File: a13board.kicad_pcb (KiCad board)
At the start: 4 copper layers, 49.8 x 45.7 mm, 124 parts, among them U1 H27UBG8T2A/TSOP48, U2 A13, U3 H5TQ2G43CFR, U4 H5TQ2G43CFR, U5 OLIMEX_IC_AXP209, U6 SY8008BAAC, U7 SY8008BAAC

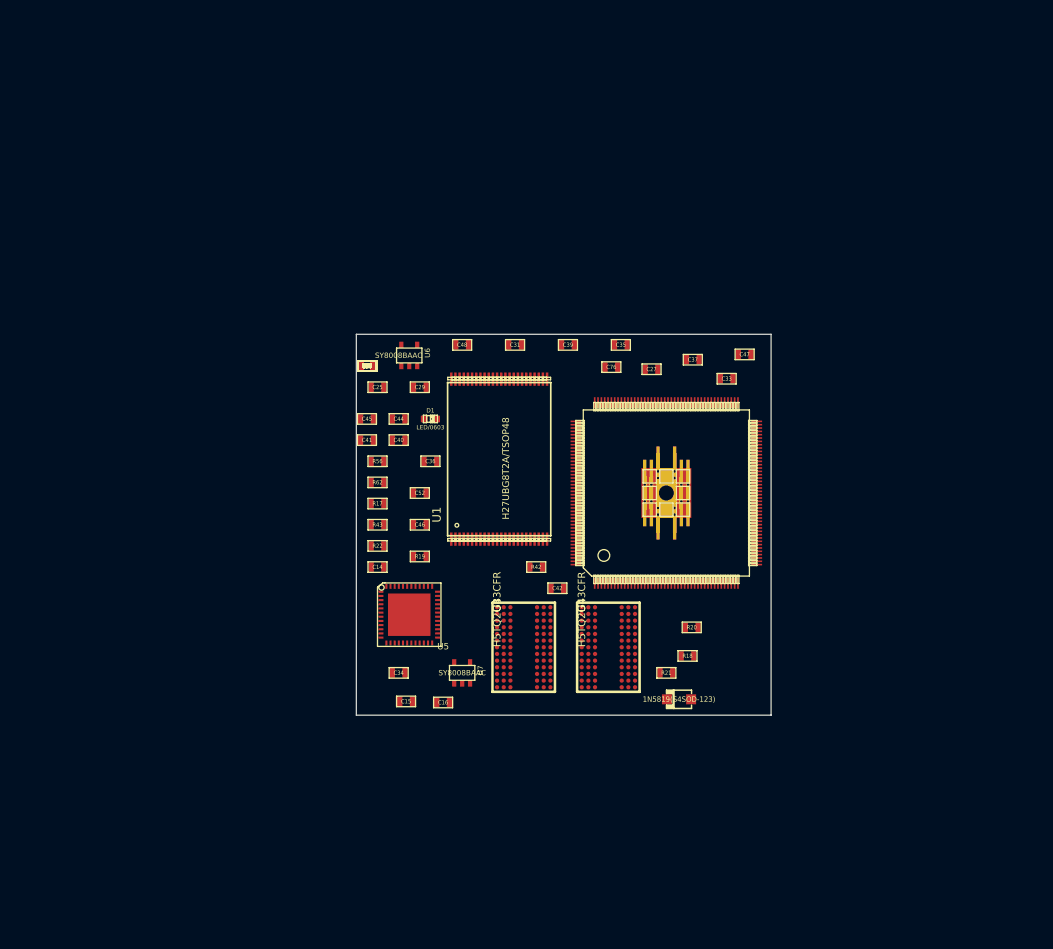
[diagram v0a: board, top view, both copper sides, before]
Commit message: fixed schematics errors, added CD32 and 4x0402 packages, started layout
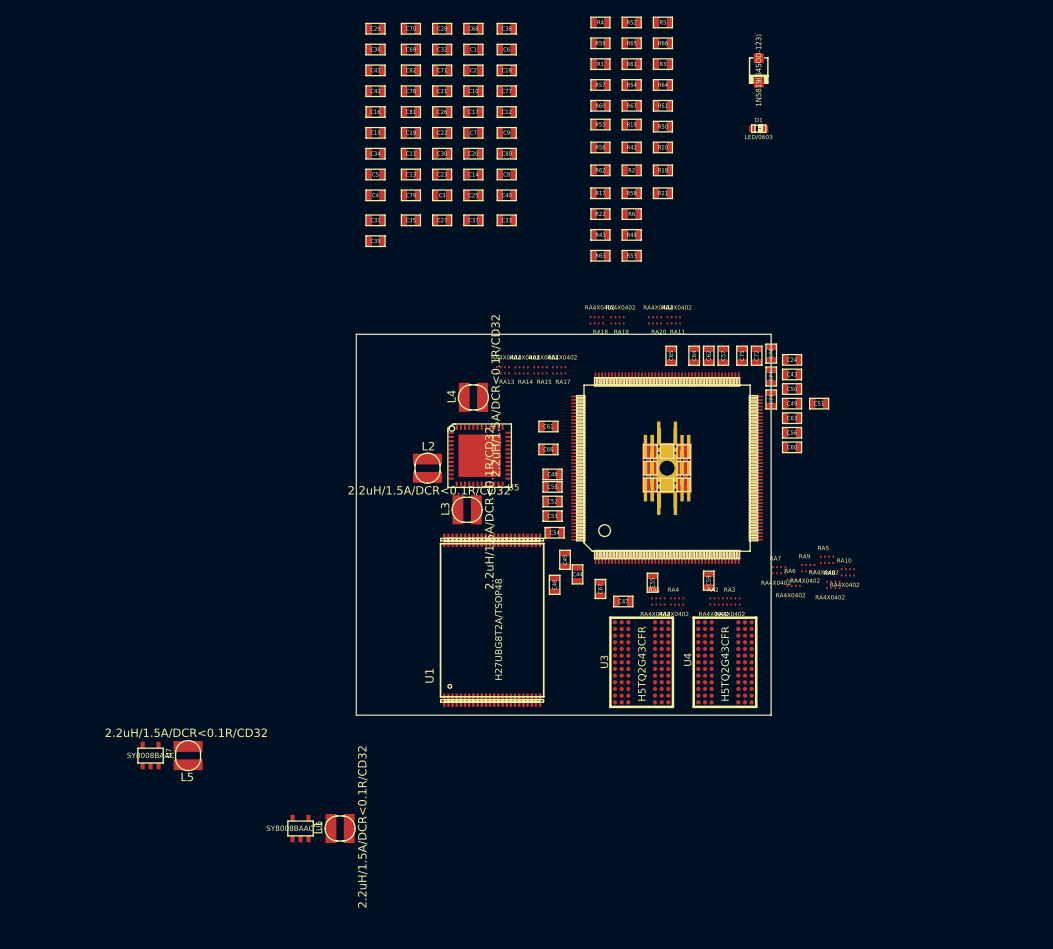
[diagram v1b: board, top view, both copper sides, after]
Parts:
- added L1: 2.2uH/1.5A/DCR<0.1R/CD32, CD32, F.Cu at (74.2, 134.2)
- added L2: 2.2uH/1.5A/DCR<0.1R/CD32, CD32, F.Cu at (84.8, 91.0)
- added L3: 2.2uH/1.5A/DCR<0.1R/CD32, CD32, F.Cu at (89.5, 96.0)
- added L4: 2.2uH/1.5A/DCR<0.1R/CD32, CD32, F.Cu at (90.2, 82.5)
- added L5: 2.2uH/1.5A/DCR<0.1R/CD32, CD32, F.Cu at (56.0, 125.5)
- added RA1: RA4X0402, RN4x0402, F.Cu at (112.5, 107.0)
- added RA10: RA4X0402, RN4x0402, F.Cu at (135.2, 103.5)
- added RA11: RA4X0402, RN4x0402, F.Cu at (114.2, 73.2)
- added RA13: RA4X0402, RN4x0402, F.Cu at (93.8, 79.2)
- added RA14: RA4X0402, RN4x0402, F.Cu at (96.0, 79.2)
- added RA15: RA4X0402, RN4x0402, F.Cu at (98.2, 79.2)
- added RA17: RA4X0402, RN4x0402, F.Cu at (100.5, 79.2)
- added RA18: RA4X0402, RN4x0402, F.Cu at (105.0, 73.2)
- added RA19: RA4X0402, RN4x0402, F.Cu at (107.5, 73.2)
- added RA2: RA4X0402, RN4x0402, F.Cu at (119.5, 107.0)
- added RA20: RA4X0402, RN4x0402, F.Cu at (112.0, 73.2)
- added RA3: RA4X0402, RN4x0402, F.Cu at (121.5, 107.0)
- added RA4: RA4X0402, RN4x0402, F.Cu at (114.8, 107.0)
- added RA5: RA4X0402, RN4x0402, F.Cu at (132.8, 102.0)
- added RA6: RA4X0402, RN4x0402, F.Cu at (128.8, 104.8)
- added RA7: RA4X0402, RN4x0402, F.Cu at (127.0, 103.2)
- added RA8: RA4X0402, RN4x0402, F.Cu at (133.5, 105.0)
- added RA9: RA4X0402, RN4x0402, F.Cu at (130.5, 103.0)
- moved D2 76.1 mm to (124.5, 43.2), turned to 90 degrees
- moved C16 71.3 mm to (78.5, 48.2)
- moved C15 68.3 mm to (78.5, 50.8)
- moved C42 63.5 mm to (78.5, 45.8), turned to 180 degrees
- moved C34 62.4 mm to (78.5, 53.2)
- moved R18 58.4 mm to (113.0, 55.2)
- moved U6 58.3 mm to (69.5, 134.2)
- moved R19 57.8 mm to (109.2, 49.8)
- moved R20 57.7 mm to (113.0, 52.5)
- moved R21 57.6 mm to (113.0, 58.0)
- moved C51 54.5 mm to (131.8, 83.2)
- moved R5 54.4 mm to (113.0, 37.5)
- moved D1 52.6 mm to (124.5, 50.2)
- moved R66 52.6 mm to (113.0, 40.0)
- moved R52 52.1 mm to (109.2, 37.5)
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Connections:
- U3 pad N8: (no net) -> /DRAM/DDR3_A8
- U4 pad N8: (no net) -> /DRAM/DDR3_A8

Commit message: Started tracing
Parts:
- moved R52 82.0 mm to (115.6, 119.3), turned to 90 degrees
- moved C2 81.5 mm to (125.6, 116.7), turned to 270 degrees
- moved C1 79.5 mm to (113.7, 116.7), turned to 270 degrees
- moved C29 78.4 mm to (65.5, 115.6), turned to 180 degrees
- moved R64 76.7 mm to (69.3, 108.1), turned to 270 degrees
- moved R66 74.6 mm to (67.9, 99.4), turned to 270 degrees
- moved C42 73.1 mm to (65.5, 117.7)
- moved C10 71.2 mm to (113.7, 113.0), turned to 90 degrees
- moved C6 69.8 mm to (122.9, 104.4), turned to 270 degrees
- moved C69 66.8 mm to (131.2, 86.7), turned to 180 degrees
- moved C68 66.6 mm to (133.9, 88.6)
- moved R56 66.6 mm to (102.9, 119.0)
- moved C9 66.4 mm to (103.6, 116.5), turned to 90 degrees
- moved C78 65.6 mm to (133.9, 86.9), turned to 180 degrees
- moved C3 65.3 mm to (115.6, 116.7), turned to 90 degrees
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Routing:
- net N-0000072: track 0.00 -> 10.4 mm
- net N-0000073: track 0.00 -> 10.1 mm
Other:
- board size 49.8 x 45.7 mm -> 99.8 x 45.7 mm
- net class Default: clearance 0.254 -> 0.1524; trace_width 0.254 -> 0.1524; via_dia 0.889 -> 0.41; via_drill 0.635 -> 0.3084
- net class signal added: clearance 0.1524, trace_width 0.1524, via_dia 0.41, via_drill 0.3084
- rule pad_to_mask_clearance: 0 -> 0.1
- rule trace_clearance: 0.254 -> 0.1524
- rule trace_min: 0.254 -> 0.1524
- rule via_min_drill: 0.508 -> 0.3
- rule via_min_size: 0.889 -> 0.4

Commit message: more tracing progress
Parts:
- C4, C44, C45, C46, C47, C48, C5, C52, C55, C56, C58, C59, C6, C60, C61, C66, C67, C68, C69, C7, C70, C78: footprint SM0603_Capa -> SM0402
- R17, R18, R19, R20, R21, R22, R42, R43, R50: footprint SM0603 -> SM0402
- moved R19 13.2 mm to (110.7, 108.0)
- moved C2 10.4 mm to (115.6, 113.9)
- moved RA3 8.43 mm to (113.2, 108.2)
- moved R42 5.51 mm to (109.9, 108.0)
- moved C54 5.33 mm to (97.3, 90.6)
- moved RA8 4.98 mm to (134.9, 102.3)
- moved D2 4.74 mm to (89.8, 93.6)
- moved R20 4.49 mm to (111.6, 108.0)
- moved C8 4.43 mm to (131.6, 94.3), turned to 315 degrees
- moved R21 4.23 mm to (117.7, 106.7)
- moved RA9 3.93 mm to (131.0, 100.6)
- moved RA1 3.58 mm to (108.5, 108.0)
- moved C47 3.42 mm to (109.8, 103.9), turned to 90 degrees
- moved R2 3.35 mm to (106.4, 107.3)
- moved C68 3.10 mm to (131.1, 87.3)
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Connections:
- net N-00000100 renamed /DRAM/CPU_BA0
- net N-00000101 renamed /DRAM/CPU_BA1
- net N-00000102 renamed /DRAM/CPU_BA2
- net N-00000103 renamed /DRAM/CPU_ODT
- net N-0000072 renamed /DRAM/CPU_CK
- net N-0000073 renamed /DRAM/CPU_CK_N
- net N-0000074 renamed /DRAM/CPU_DM1
- net N-0000075 renamed /DRAM/CPU_MEMRST
- net N-0000076 renamed /DRAM/CPU_WE
- net N-0000077 renamed /DRAM/CPU_CKE
- net N-0000078 renamed /DRAM/CPU_CAS
- net N-0000079 renamed /DRAM/CPU_RAS
- net N-0000080 renamed /DRAM/CPU_DM0
- net N-0000081 renamed /DRAM/CPU_A6
- net N-0000082 renamed /DRAM/CPU_DQS0
- net N-0000083 renamed /DRAM/CPU_DQS0_N
- net N-0000084 renamed /DRAM/CPU_DQS1
- net N-0000085 renamed /DRAM/CPU_DQS1_N
- net N-0000086 renamed /DRAM/CPU_A0
- net N-0000087 renamed /DRAM/CPU_A1
- net N-0000088 renamed /DRAM/CPU_A2
- net N-0000089 renamed /DRAM/CPU_A3
- net N-0000090 renamed /DRAM/CPU_A4
- net N-0000091 renamed /DRAM/CPU_A5
- net N-0000092 renamed /DRAM/CPU_A7
- net N-0000093 renamed /DRAM/CPU_A8
- net N-0000094 renamed /DRAM/CPU_A9
- net N-0000095 renamed /DRAM/CPU_A10
- net N-0000096 renamed /DRAM/CPU_A11
- net N-0000097 renamed /DRAM/CPU_A12
- net N-0000098 renamed /DRAM/CPU_A13
- net N-0000099 renamed /DRAM/CPU_A14
- RA1 pad 1: /DRAM/DDR3_D0 -> /DRAM/CPU_D0
- RA1 pad 2: /DRAM/DDR3_D2 -> /DRAM/CPU_D2
- RA1 pad 3: /DRAM/DDR3_D6 -> /DRAM/CPU_D6
- RA1 pad 4: /DRAM/DDR3_D4 -> /DRAM/CPU_D4
- RA1 pad 5: N-0000056 -> /DRAM/DDR3_D4
- RA1 pad 6: N-0000062 -> /DRAM/DDR3_D6
- RA1 pad 7: N-0000059 -> /DRAM/DDR3_D2
- RA1 pad 8: N-0000057 -> /DRAM/DDR3_D0
- RA2 pad 1: /DRAM/DDR3_D10 -> /DRAM/CPU_D10
- RA2 pad 2: /DRAM/DDR3_D14 -> /DRAM/CPU_D14
- RA2 pad 3: /DRAM/DDR3_D8 -> /DRAM/CPU_D8
- RA2 pad 4: /DRAM/DDR3_D12 -> /DRAM/CPU_D12
- RA2 pad 5: N-0000068 -> /DRAM/DDR3_D12
- RA2 pad 6: N-0000064 -> /DRAM/DDR3_D8
- RA2 pad 7: N-0000070 -> /DRAM/DDR3_D14
- RA2 pad 8: N-0000066 -> /DRAM/DDR3_D10
- RA3 pad 1: /DRAM/DDR3_D5 -> /DRAM/CPU_D5
- RA3 pad 2: /DRAM/DDR3_D7 -> /DRAM/CPU_D7
- RA3 pad 3: /DRAM/DDR3_D3 -> /DRAM/CPU_D3
- RA3 pad 4: /DRAM/DDR3_D1 -> /DRAM/CPU_D1
- RA3 pad 5: N-0000058 -> /DRAM/DDR3_D1
- RA3 pad 6: N-0000060 -> /DRAM/DDR3_D3
- RA3 pad 7: N-0000063 -> /DRAM/DDR3_D7
- RA3 pad 8: N-0000061 -> /DRAM/DDR3_D5
- RA4 pad 1: /DRAM/DDR3_D15 -> /DRAM/CPU_D15
- RA4 pad 2: /DRAM/DDR3_D13 -> /DRAM/CPU_D13
- RA4 pad 3: /DRAM/DDR3_D9 -> /DRAM/CPU_D9
- RA4 pad 4: /DRAM/DDR3_D11 -> /DRAM/CPU_D11
- RA4 pad 5: N-0000067 -> /DRAM/DDR3_D11
- RA4 pad 6: N-0000065 -> /DRAM/DDR3_D9
- RA4 pad 7: N-0000069 -> /DRAM/DDR3_D13
- RA4 pad 8: N-0000071 -> /DRAM/DDR3_D15
- U2 pad 19: N-0000056 -> /DRAM/CPU_D4
- U2 pad 20: N-0000062 -> /DRAM/CPU_D6
- U2 pad 21: N-0000059 -> /DRAM/CPU_D2
- U2 pad 22: N-0000057 -> /DRAM/CPU_D0
- U2 pad 24: N-0000067 -> /DRAM/CPU_D11
- U2 pad 25: N-0000065 -> /DRAM/CPU_D9
- U2 pad 26: N-0000069 -> /DRAM/CPU_D13
- U2 pad 27: N-0000071 -> /DRAM/CPU_D15
- U2 pad 36: N-0000068 -> /DRAM/CPU_D12
- U2 pad 37: N-0000064 -> /DRAM/CPU_D8
- U2 pad 38: N-0000070 -> /DRAM/CPU_D14
- U2 pad 39: N-0000066 -> /DRAM/CPU_D10
- U2 pad 40: N-0000058 -> /DRAM/CPU_D1
- U2 pad 41: N-0000060 -> /DRAM/CPU_D3
- U2 pad 42: N-0000063 -> /DRAM/CPU_D7
- U2 pad 44: N-0000061 -> /DRAM/CPU_D5
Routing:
- net /DRAM/DDR3_A7: track 0.00 -> 47.7 mm, vias 0 -> 2
- net /DRAM/DDR3_RST: track 0.00 -> 45.0 mm
- net /DRAM/DDR3_A9: track 0.00 -> 44.6 mm, vias 0 -> 2
- net /DRAM/DDR3_A5: track 0.00 -> 40.3 mm, vias 0 -> 2
- net /DRAM/DDR3_BA0: track 0.00 -> 39.3 mm, vias 0 -> 2
- net /DRAM/DDR3_A13: track 0.00 -> 39.3 mm
- net /DRAM/DDR3_A0: track 0.00 -> 38.9 mm
- net /DRAM/DDR3_A3: track 0.00 -> 38.1 mm, vias 0 -> 2
- net /DRAM/DDR3_BA2: track 0.00 -> 38.0 mm
- net /DRAM/DDR3_A2: track 0.00 -> 37.7 mm
- net /DRAM/DDR3_WE: track 0.00 -> 37.7 mm
- net /DRAM/DDR3_CAS: track 0.00 -> 35.5 mm
- net /DRAM/DDR3_RAS: track 0.00 -> 35.1 mm
- net /DRAM/DDR3_A11: track 0.00 -> 26.9 mm
- net N-00000190: track 0.00 -> 26.3 mm
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- added copper zone on Inner1.Cu, net GND
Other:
- net class Default: via_dia 0.41 -> 0.31; via_drill 0.3084 -> 0.3048
- net class bga added: clearance 0.1016, trace_width 0.1016, via_dia 0.31, via_drill 0.3048
- net class signal: via_dia 0.41 -> 0.31; via_drill 0.3084 -> 0.3048
- rule trace_min: 0.1524 -> 0.1016
- rule via_min_size: 0.4 -> 0.3048

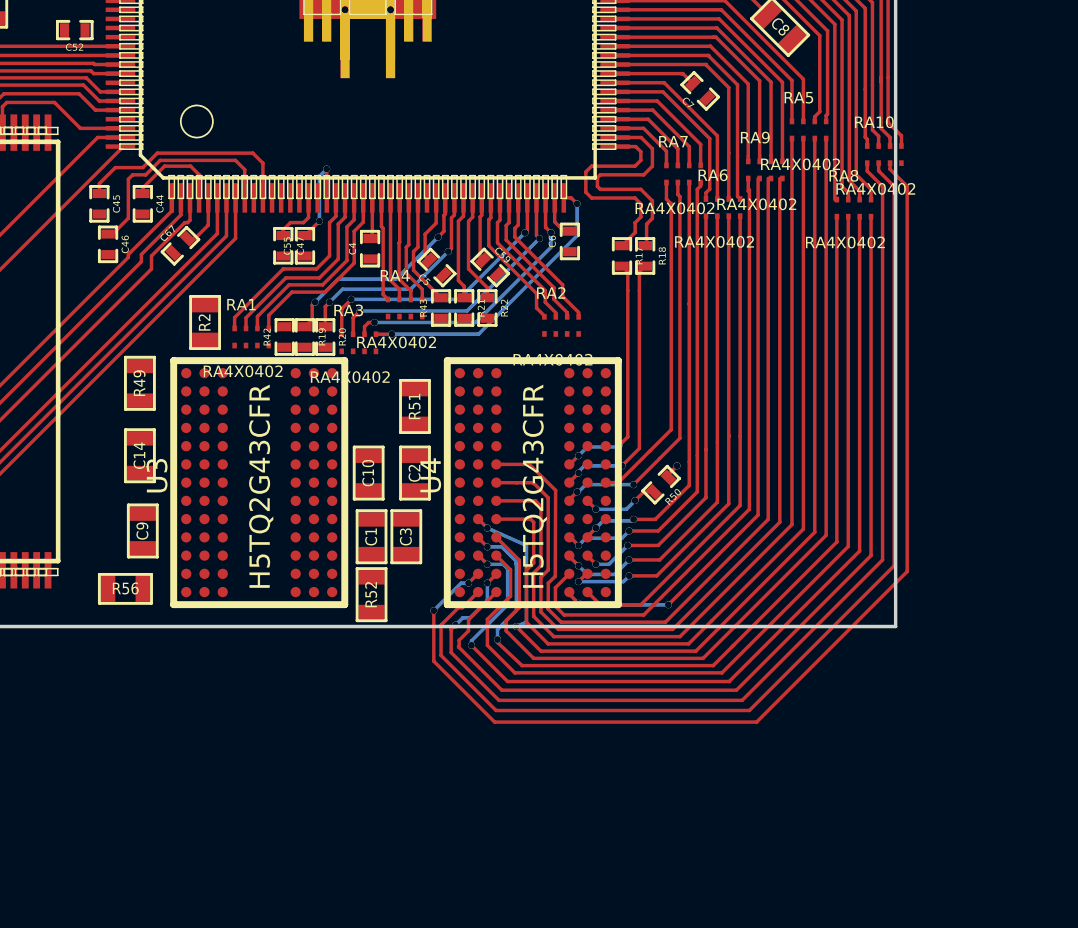
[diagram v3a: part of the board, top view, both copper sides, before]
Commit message: Re-tracing DDR3 with 4mil traces
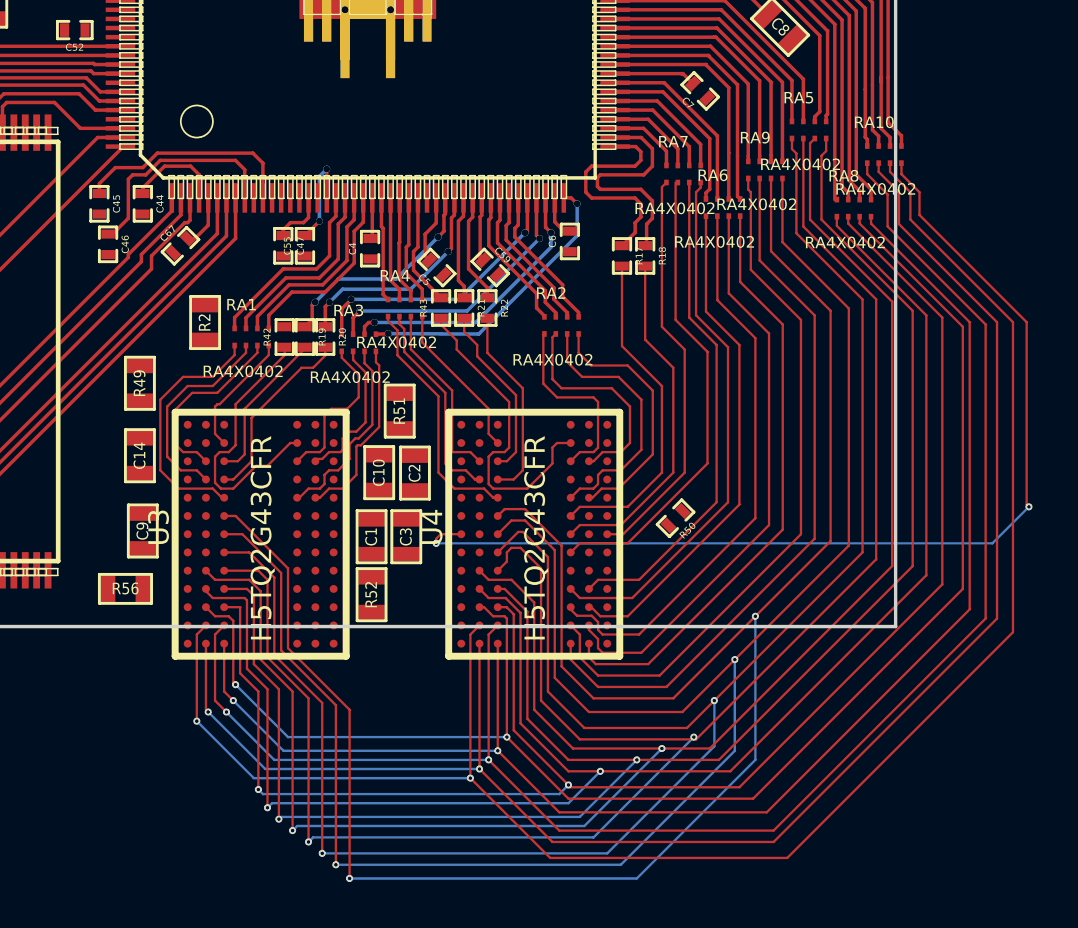
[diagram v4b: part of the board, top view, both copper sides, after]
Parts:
- moved U3 2.26 mm to (105.6, 111.8)
- moved U4 2.26 mm to (117.6, 111.8)
- moved R50 1.60 mm to (127.0, 115.9)
- moved R51 0.70 mm to (114.9, 111.2)
- moved C10 0.46 mm to (114.0, 113.9)
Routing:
- net /DRAM/DDR3_RAS: track 35.1 -> 85.8 mm, vias 0 -> 2
- net /DRAM/DDR3_CAS: track 35.5 -> 83.3 mm, vias 0 -> 2
- net /DRAM/DDR3_ODT: track 0.00 -> 45.4 mm, vias 0 -> 2
- net /DRAM/DDR3_WE: track 37.7 -> 82.8 mm, vias 0 -> 2
- net /DRAM/DDR3_BA2: track 38.0 -> 80.3 mm, vias 0 -> 2
- net /DRAM/DDR3_BA0: track 39.3 -> 79.3 mm
- net /DRAM/DDR3_A0: track 38.9 -> 76.5 mm, vias 0 -> 2
- net /DRAM/DDR3_A3: track 38.1 -> 73.5 mm
- net /DRAM/DDR3_A2: track 37.7 -> 70.2 mm, vias 0 -> 2
- net /DRAM/DDR3_A7: track 47.7 -> 76.4 mm
- net /DRAM/DDR3_A9: track 44.6 -> 71.7 mm
- net /DRAM/DDR3_A5: track 40.3 -> 67.0 mm
- net /DRAM/DDR3_RST: track 45.0 -> 71.7 mm, vias 0 -> 2
- net /DRAM/DDR3_A13: track 39.3 -> 64.4 mm, vias 0 -> 2
- net /DRAM/DDR3_DM1: track 0.00 -> 14.1 mm
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- removed copper zone on Inner1.Cu, net GND
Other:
- net class Default: clearance 0.1524 -> 0.15; trace_width 0.1524 -> 0.15; via_drill 0.3048 -> 0.3
- net class bga: via_drill 0.3048 -> 0.3
- net class signal removed
- rule trace_clearance: 0.1524 -> 0.15
- rule via_min_size: 0.3048 -> 0.3

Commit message: still routing ddr3
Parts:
- moved L5 11.4 mm to (74.7, 101.0)
- moved C40 11.1 mm to (80.0, 104.5)
- moved R66 11.1 mm to (77.9, 104.5)
- moved U7 11.1 mm to (79.5, 101.0)
- moved R67 10.5 mm to (83.4, 101.0)
- moved C39 8.39 mm to (85.7, 101.0)
- moved C41 7.82 mm to (85.7, 103.9)
- moved R56 7.81 mm to (95.1, 120.0)
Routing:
- net /DRAM/DDR3_A7: track 76.4 -> 0.00 mm, vias 2 -> 0
- net /DRAM/DDR3_A9: track 71.7 -> 0.00 mm, vias 2 -> 0
- net /DRAM/DDR3_RST: track 71.7 -> 0.14 mm, vias 2 -> 0
- net /DRAM/DDR3_A2: track 70.2 -> 0.00 mm, vias 2 -> 0
- net /DRAM/DDR3_A5: track 67.0 -> 0.00 mm, vias 2 -> 0
- net /DRAM/DDR3_A13: track 64.4 -> 0.00 mm, vias 2 -> 0
- net VMEM: track 17.4 -> 75.6 mm, vias 0 -> 14
- net /DRAM/DDR3_RAS: track 85.8 -> 64.9 mm
- net /DRAM/DDR3_CAS: track 83.3 -> 65.0 mm
- net /DRAM/DDR3_WE: track 82.8 -> 66.6 mm
- net /DRAM/DDR3_A11: track 30.7 -> 45.5 mm, vias 0 -> 2
- net /DRAM/DDR3_A14: track 31.4 -> 45.9 mm, vias 0 -> 2
- net /DRAM/DDR3_A8: track 26.2 -> 39.6 mm, vias 0 -> 2
- net /DRAM/DDR3_BA2: track 80.3 -> 67.5 mm
- net /DRAM/DDR3_BA0: track 79.3 -> 69.7 mm
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- added copper zone on Inner1.Cu, net VMEM
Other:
- board size 99.8 x 45.7 mm -> 122.3 x 91.1 mm
- net class Default: via_dia 0.31 -> 0.6
- net class bga: via_dia 0.31 -> 0.6
- net class power added: clearance 2, trace_width 0.2, via_dia 0.6, via_drill 0.3
- net class powersm added: clearance 0.15, trace_width 0.2, via_dia 0.6, via_drill 0.3
- rule via_min_size: 0.3 -> 0.6
